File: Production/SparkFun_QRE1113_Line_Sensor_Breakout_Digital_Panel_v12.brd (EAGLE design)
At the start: 135.1 x 85.6 mm, 678 parts, among them U1 QRE1113, U10 QRE1113, U11 QRE1113, U12 QRE1113, U13 QRE1113, U14 QRE1113, U15 QRE1113, U16 QRE1113, U17 QRE1113, U18 QRE1113, U19 QRE1113, U2 QRE1113, U20 QRE1113, U21 QRE1113, U22 QRE1113, U23 QRE1113, U24 QRE1113, U25 QRE1113, U26 QRE1113, U27 QRE1113, U28 QRE1113, U29 QRE1113, U3 QRE1113, U30 QRE1113, U31 QRE1113, U32 QRE1113, U33 QRE1113, U34 QRE1113, U35 QRE1113, U36 QRE1113, U37 QRE1113, U38 QRE1113, U39 QRE1113, U4 QRE1113, U40 QRE1113, U41 QRE1113, U42 QRE1113, U43 QRE1113, U44 QRE1113, U45 QRE1113, U46 QRE1113, U47 QRE1113, U48 QRE1113, U49 QRE1113, U5 QRE1113, U50 QRE1113, U51 QRE1113, U52 QRE1113, U53 QRE1113, U54 QRE1113, U55 QRE1113, U56 QRE1113, U57 QRE1113, U58 QRE1113, U59 QRE1113, U6 QRE1113, U60 QRE1113, U61 QRE1113, U62 QRE1113, U63 QRE1113, U64 QRE1113, U65 QRE1113, U66 QRE1113, U67 QRE1113, U68 QRE1113, U69 QRE1113, U7 QRE1113, U70 QRE1113, U71 QRE1113, U72 QRE1113, U73 QRE1113, U74 QRE1113, U75 QRE1113, U8 QRE1113, U9 QRE1113

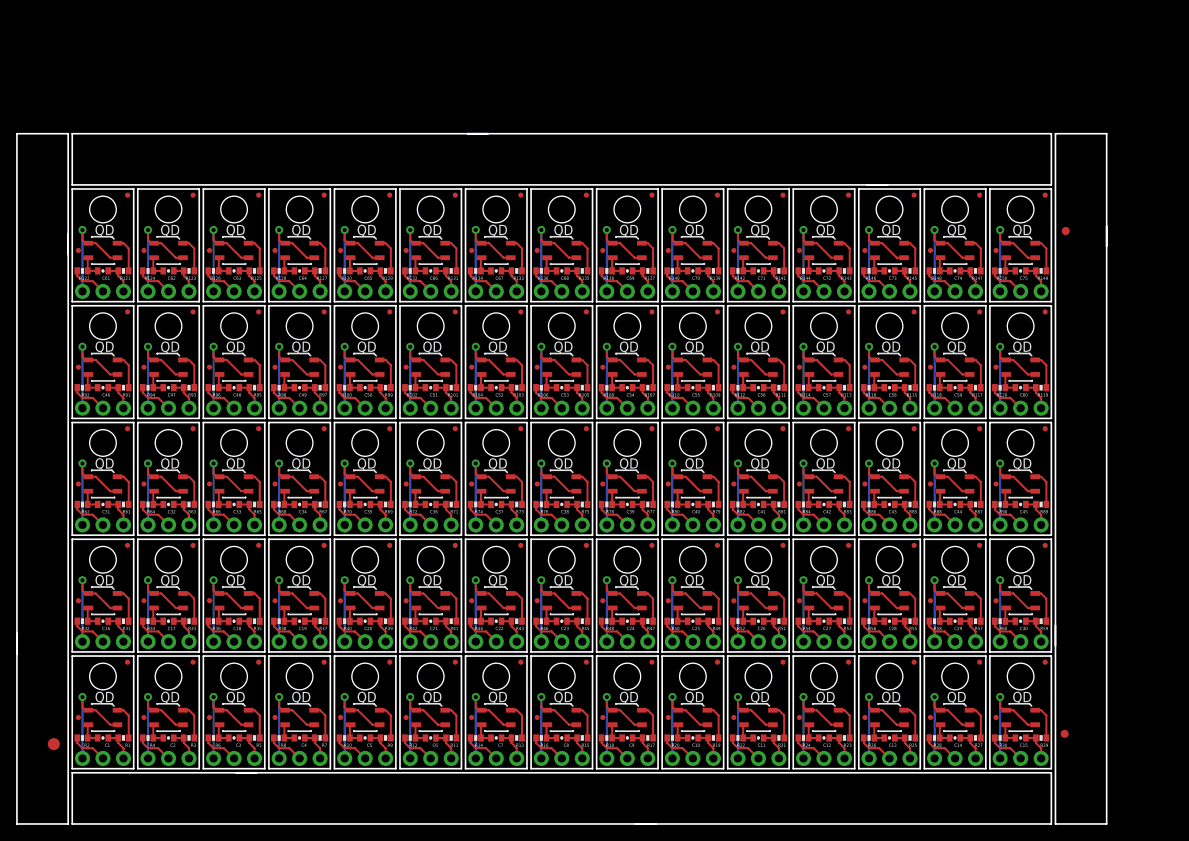
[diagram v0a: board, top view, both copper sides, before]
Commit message: made panel bigger
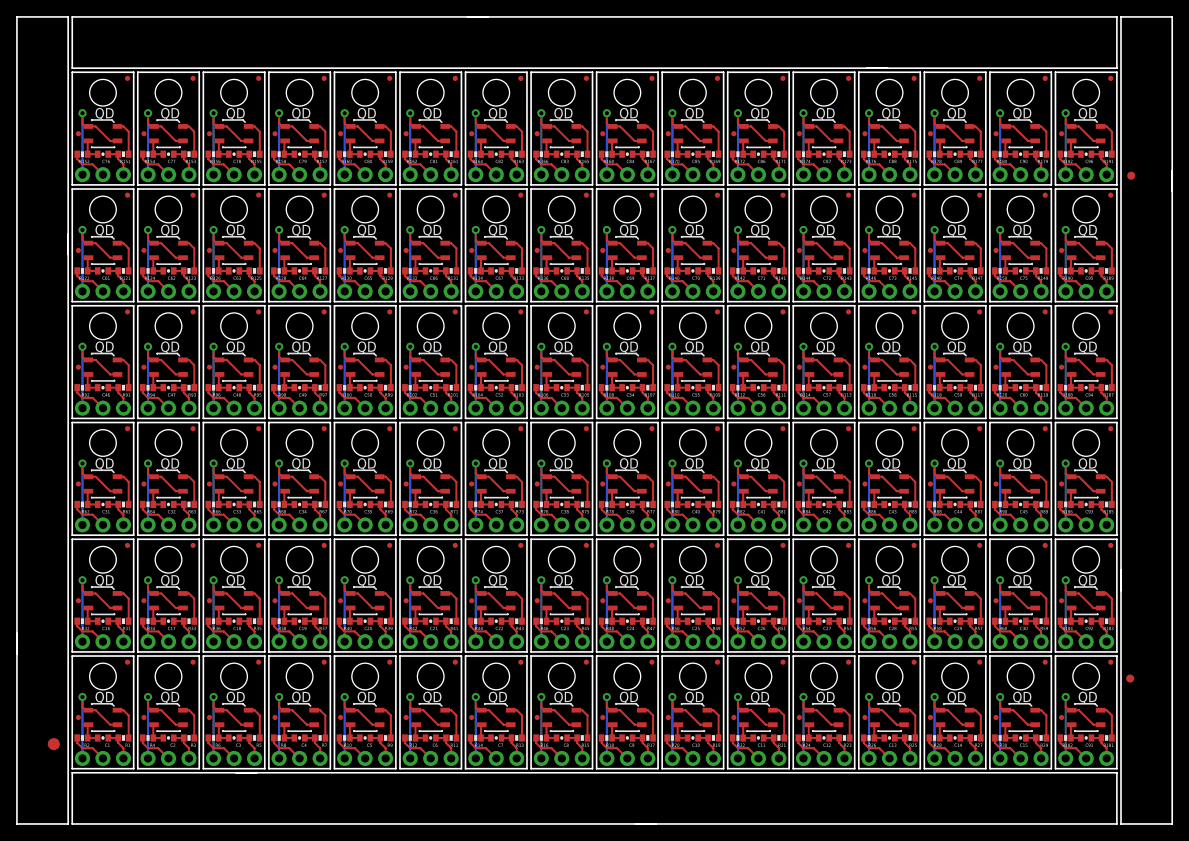
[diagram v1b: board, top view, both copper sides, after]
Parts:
- added C76, C77, C78, C79, C80, C81, C82, C83, C84, C85, C86, C87, C88, C89, C90, C91, C92, C93, C94, C95, C96: 10nF, SparkFun:0402-CAP
- added FID151, FID152, FID153, FID154, FID155, FID156, FID157, FID158, FID159, FID160, FID161, FID162, FID163, FID164, FID165, FID166, FID167, FID168, FID169, FID170, FID171, FID172, FID173, FID174, FID175, FID176, FID177, FID178, FID179, FID180, FID181, FID182, FID183, FID184, FID185, FID186, FID187, FID188, FID189, FID190, FID191, FID192: FIDUCIALUFIDUCIAL, SparkFun-Aesthetics:MICRO-FIDUCIAL
- added JP226, JP229, JP232, JP235, JP238, JP241, JP244, JP247, JP250, JP253, JP256, JP259, JP262, JP265, JP268, JP271, JP274, JP277, JP280, JP283, JP286: (no value), SparkFun:1X03
- added JP227, JP230, JP233, JP236, JP239, JP242, JP245, JP248, JP251, JP254, JP257, JP260, JP263, JP266, JP269, JP272, JP275, JP278, JP281, JP284, JP287: LOGO-SFESK, SparkFun:SFE-LOGO-FLAME
- added JP228, JP231, JP234, JP237, JP240, JP243, JP246, JP249, JP252, JP255, JP258, JP261, JP264, JP267, JP270, JP273, JP276, JP279, JP282, JP285, JP288: STAND-OFF, SparkFun:STAND-OFF
- added R151, R153, R155, R157, R159, R161, R163, R165, R167, R169, R171, R173, R175, R177, R179, R181, R183, R185, R187, R189, R191: 100, SparkFun:0402-RES
- added R152, R154, R156, R158, R160, R162, R164, R166, R168, R170, R172, R174, R176, R178, R180, R182, R184, R186, R188, R190, R192: 220, SparkFun:0402-RES
- added U76, U77, U78, U79, U80, U81, U82, U83, U84, U85, U86, U87, U88, U89, U90, U91, U92, U93, U94, U95, U96: QRE1113, SparkFun:QRE1113
- moved E$5 10.6 mm to (138.0, 18.0)
- moved E$7 10.6 mm to (138.2, 80.4)
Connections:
- new net GND75: JP226.3, U76.2, U76.4
- new net GND76: JP229.3, U77.2, U77.4
- new net GND77: JP232.3, U78.2, U78.4
- new net GND78: JP235.3, U79.2, U79.4
- new net GND79: JP238.3, U80.2, U80.4
- new net GND80: JP241.3, U81.2, U81.4
- new net GND81: JP244.3, U82.2, U82.4
- new net GND82: JP247.3, U83.2, U83.4
- new net GND83: JP250.3, U84.2, U84.4
- new net GND84: JP253.3, U85.2, U85.4
- new net GND85: JP256.3, U86.2, U86.4
- new net GND86: JP259.3, U87.2, U87.4
- new net GND87: JP262.3, U88.2, U88.4
- new net GND88: JP265.3, U89.2, U89.4
- new net GND89: JP268.3, U90.2, U90.4
- new net GND90: JP271.3, U91.2, U91.4
- new net GND91: JP274.3, U92.2, U92.4
- new net GND92: JP277.3, U93.2, U93.4
- new net GND93: JP280.3, U94.2, U94.4
- new net GND94: JP283.3, U95.2, U95.4
- new net GND95: JP286.3, U96.2, U96.4
- new net N$76: R151.1, U76.1
- new net N$77: R153.1, U77.1
- new net N$78: R155.1, U78.1
- new net N$79: R157.1, U79.1
- new net N$80: R159.1, U80.1
- new net N$81: R161.1, U81.1
- new net N$82: R163.1, U82.1
- new net N$83: R165.1, U83.1
- new net N$84: R167.1, U84.1
- new net N$85: R169.1, U85.1
- new net N$86: R171.1, U86.1
- new net N$87: R173.1, U87.1
- new net N$88: R175.1, U88.1
- new net N$89: R177.1, U89.1
- new net N$90: R179.1, U90.1
- new net N$91: R181.1, U91.1
- new net N$92: R183.1, U92.1
- new net N$93: R185.1, U93.1
- new net N$94: R187.1, U94.1
- new net N$95: R189.1, U95.1
- new net N$96: R191.1, U96.1
- new net OUT150: C76.2, R152.1, U76.3
- new net OUT151: JP226.2, R152.2
- new net OUT152: C77.2, R154.1, U77.3
- new net OUT153: JP229.2, R154.2
- new net OUT154: C78.2, R156.1, U78.3
- new net OUT155: JP232.2, R156.2
- new net OUT156: C79.2, R158.1, U79.3
- new net OUT157: JP235.2, R158.2
- new net OUT158: C80.2, R160.1, U80.3
- new net OUT159: JP238.2, R160.2
- new net OUT160: C81.2, R162.1, U81.3
- new net OUT161: JP241.2, R162.2
- new net OUT162: C82.2, R164.1, U82.3
- new net OUT163: JP244.2, R164.2
- new net OUT164: C83.2, R166.1, U83.3
- new net OUT165: JP247.2, R166.2
- new net OUT166: C84.2, R168.1, U84.3
- new net OUT167: JP250.2, R168.2
- new net OUT168: C85.2, R170.1, U85.3
- new net OUT169: JP253.2, R170.2
- new net OUT170: C86.2, R172.1, U86.3
- new net OUT171: JP256.2, R172.2
- new net OUT172: C87.2, R174.1, U87.3
- new net OUT173: JP259.2, R174.2
- new net OUT174: C88.2, R176.1, U88.3
- new net OUT175: JP262.2, R176.2
- new net OUT176: C89.2, R178.1, U89.3
- new net OUT177: JP265.2, R178.2
- new net OUT178: C90.2, R180.1, U90.3
- new net OUT179: JP268.2, R180.2
- new net OUT180: C91.2, R182.1, U91.3
- new net OUT181: JP271.2, R182.2
- new net OUT182: C92.2, R184.1, U92.3
- new net OUT183: JP274.2, R184.2
- new net OUT184: C93.2, R186.1, U93.3
- new net OUT185: JP277.2, R186.2
- new net OUT186: C94.2, R188.1, U94.3
- new net OUT187: JP280.2, R188.2
- new net OUT188: C95.2, R190.1, U95.3
- new net OUT189: JP283.2, R190.2
- new net OUT190: C96.2, R192.1, U96.3
- new net OUT191: JP286.2, R192.2
- new net VCC75: C76.1, JP226.1, R151.2
- new net VCC76: C77.1, JP229.1, R153.2
- new net VCC77: C78.1, JP232.1, R155.2
- new net VCC78: C79.1, JP235.1, R157.2
- new net VCC79: C80.1, JP238.1, R159.2
- new net VCC80: C81.1, JP241.1, R161.2
- new net VCC81: C82.1, JP244.1, R163.2
- new net VCC82: C83.1, JP247.1, R165.2
- new net VCC83: C84.1, JP250.1, R167.2
- new net VCC84: C85.1, JP253.1, R169.2
- new net VCC85: C86.1, JP256.1, R171.2
- new net VCC86: C87.1, JP259.1, R173.2
- new net VCC87: C88.1, JP262.1, R175.2
- new net VCC88: C89.1, JP265.1, R177.2
- new net VCC89: C90.1, JP268.1, R179.2
- new net VCC90: C91.1, JP271.1, R181.2
- new net VCC91: C92.1, JP274.1, R183.2
- new net VCC92: C93.1, JP277.1, R185.2
- new net VCC93: C94.1, JP280.1, R187.2
- new net VCC94: C95.1, JP283.1, R189.2
- new net VCC95: C96.1, JP286.1, R191.2
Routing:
- net GND89: track 0.00 -> 14.1 mm, vias 0 -> 1
- net GND88: track 0.00 -> 14.1 mm, vias 0 -> 1
- net GND87: track 0.00 -> 14.1 mm, vias 0 -> 1
- net GND86: track 0.00 -> 14.1 mm, vias 0 -> 1
- net GND85: track 0.00 -> 14.1 mm, vias 0 -> 1
- net GND84: track 0.00 -> 14.1 mm, vias 0 -> 1
- net GND83: track 0.00 -> 14.1 mm, vias 0 -> 1
- net GND82: track 0.00 -> 14.1 mm, vias 0 -> 1
- net GND77: track 0.00 -> 14.1 mm, vias 0 -> 1
- net GND76: track 0.00 -> 14.1 mm, vias 0 -> 1
- net GND75: track 0.00 -> 14.1 mm, vias 0 -> 1
- net GND95: track 0.00 -> 14.1 mm, vias 0 -> 1
- net GND81: track 0.00 -> 14.1 mm, vias 0 -> 1
- net GND80: track 0.00 -> 14.1 mm, vias 0 -> 1
- net GND79: track 0.00 -> 14.1 mm, vias 0 -> 1
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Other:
- board size 135.1 x 85.6 mm -> 143.3 x 100.1 mm
